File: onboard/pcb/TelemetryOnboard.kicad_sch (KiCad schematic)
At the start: 138 parts, among them J1 USB-C, J2 USB-C, J3 RFPC-SMA28-F, J4 RFPC-SMA28-F, J5 Molex_MicroFit_2pin, M1 M4 Mounting Hole, M2 M4 Mounting Hole, M3 M4 Mounting Hole, M4 M4 Mounting Hole, Q1 NPN, U1 CP2102N, U2 CP2102N, U3 RC1780HP-RC232, U4 RC1701HP-RC232, U5 AVR128DB64x-xPT, U6 W25Q80DVSSIG

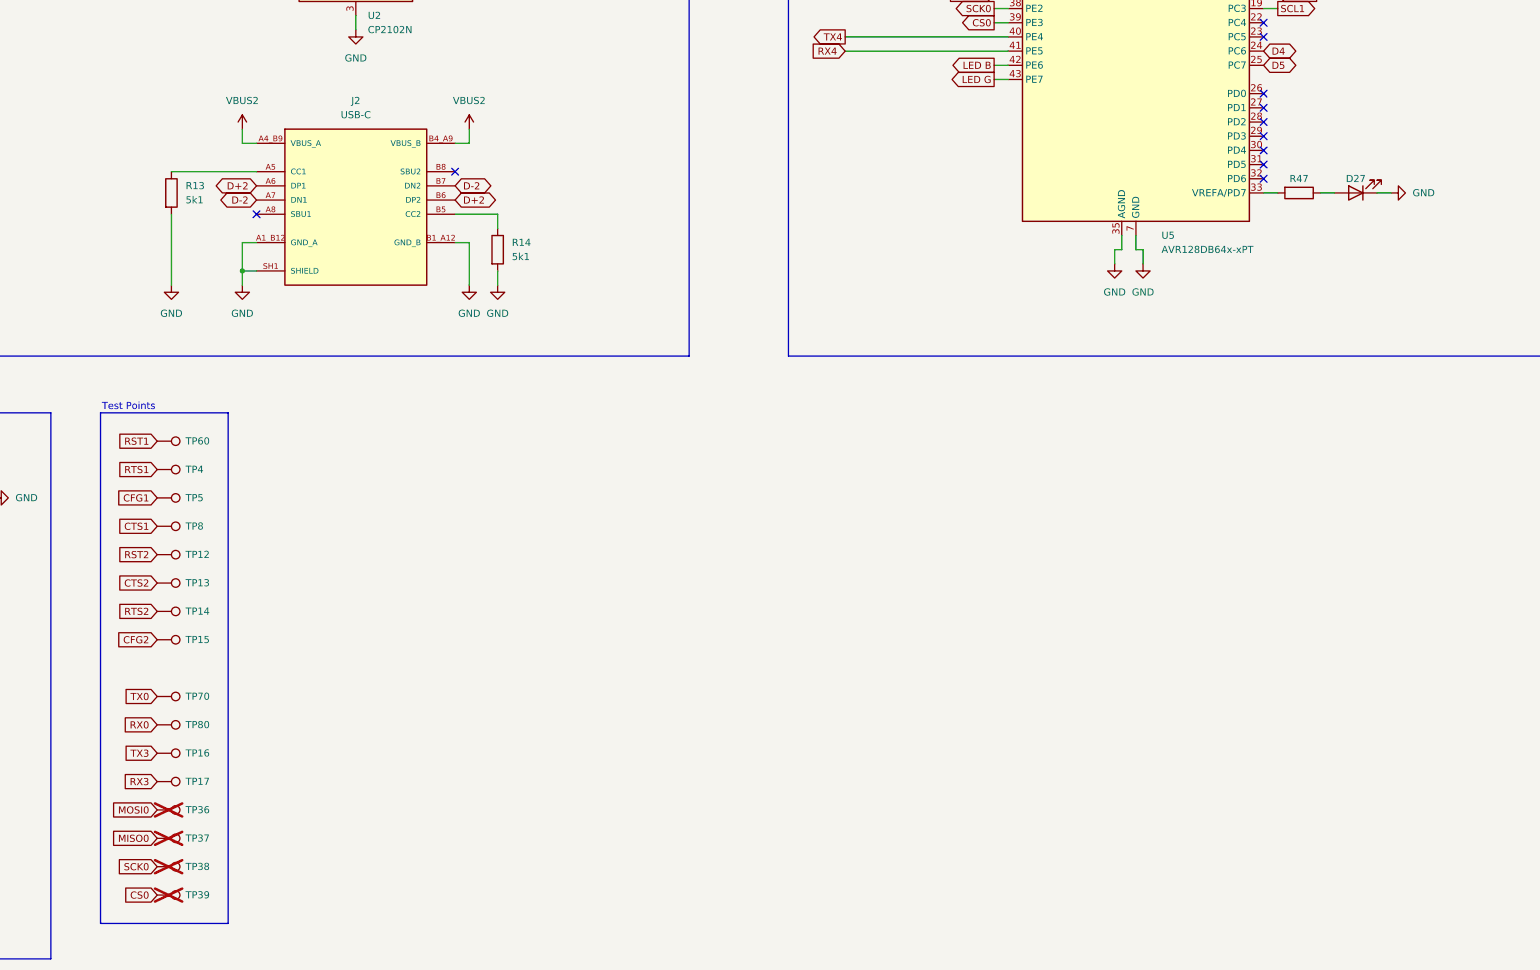
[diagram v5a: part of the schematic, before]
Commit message: improve pcb layout
include for example LEDs for three subsystems
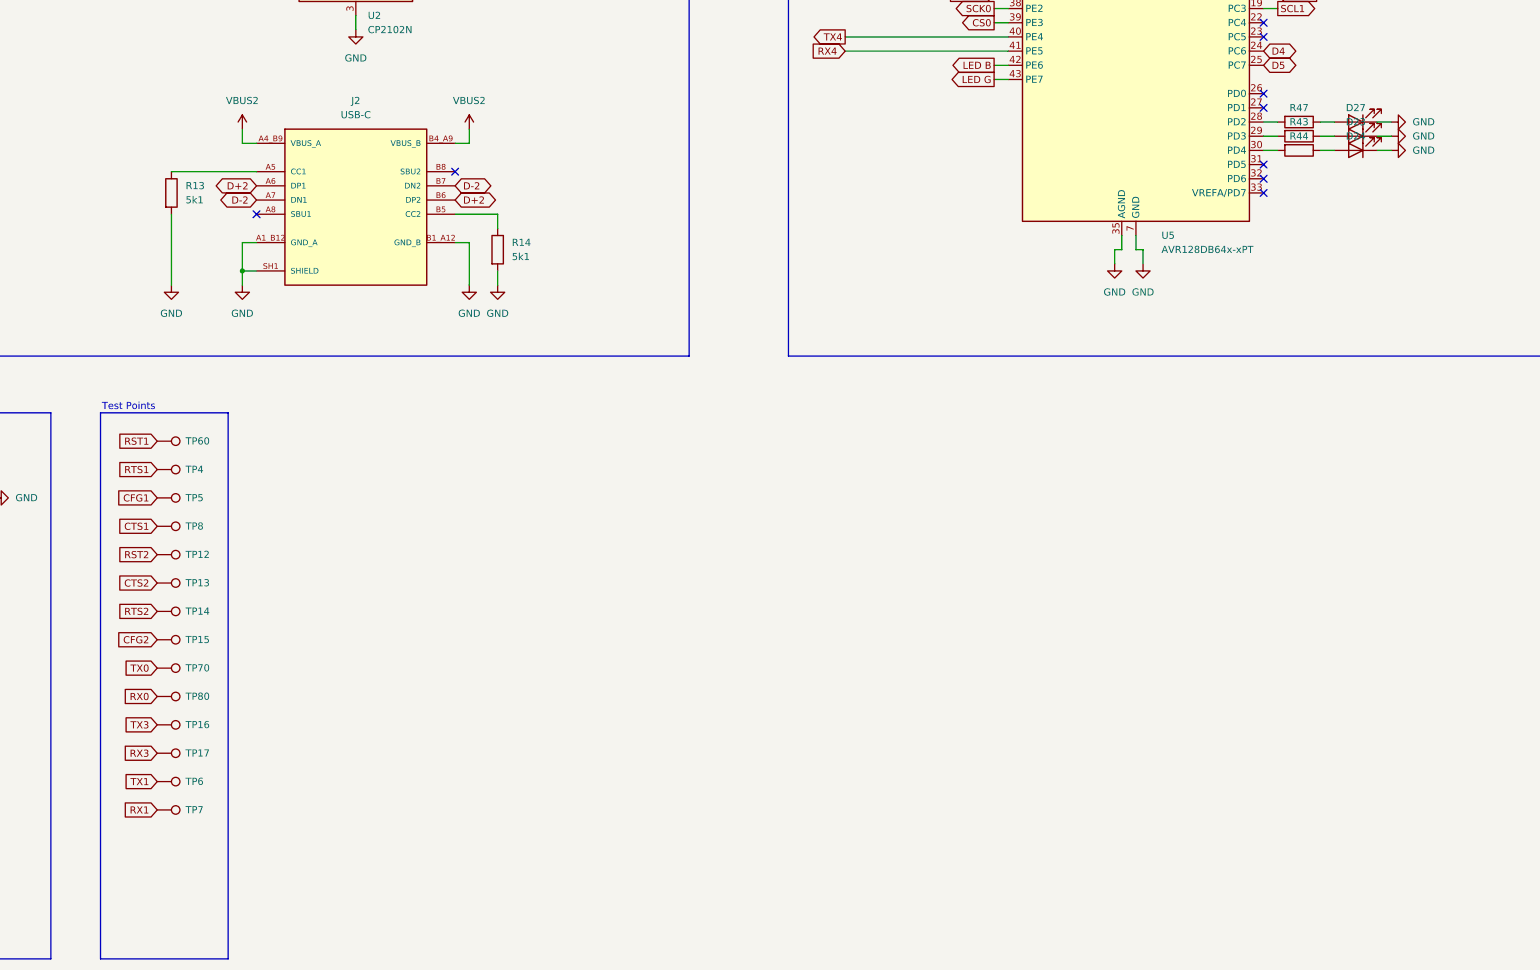
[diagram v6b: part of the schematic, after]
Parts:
- removed TP36, TP37, TP38, TP39: TestPoint, Footprints:Test Point, symbol Connector:TestPoint
- added D23, D24: orange, LED_SMD:LED_0805_2012Metric_Pad1.15x1.40mm_HandSolder, symbol Device:LED
- added R43, R44: 270R, Resistor_SMD:R_0805_2012Metric_Pad1.20x1.40mm_HandSolder, symbol Device:R
- added TP6, TP7: TestPoint, Footprints:Test Point, symbol Connector:TestPoint
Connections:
- net GND: now also D23.1 (K), D24.1 (K)
- net RX1: now also TP7.1
- net TX1: now also TP6.1
- net at U5.28 (PD2): now also R47.2
- net at U5.29 (PD3): now also R43.2
- net at U5.30 (PD4): now also R44.2
- net at U5.33 (VREFA/PD7): no longer R47.2
- new net: D24.2 (A), R44.1
- new net: D23.2 (A), R43.1
- no-connect marks 40 -> 38
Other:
- moved on the sheet: D27, R47, TP16, TP17, TP70, TP80

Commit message: smal updates and component annotation
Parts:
- removed TP4, TP5, TP60: TestPoint, Footprints:Test Point, symbol Connector:TestPoint
- added TP15, TP16, TP17: TestPoint, Footprints:Test Point, symbol Connector:TestPoint
- C10: renamed from C6; value 1 uf -> 1 uF
- C11: renamed from C7; Purchase-URL https://www.digikey.de/de/products/detail/samsung-electro-m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 -> (none)
- C12: renamed from C8; value 1 uf -> 1 uF
- C13: renamed from C15; value 1 uf -> 1 uF
- C5: renamed from C9; Purchase-URL https://www.digikey.de/de/products/detail/samsung-electro-m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 -> (none)
- C6: renamed from C10; Purchase-URL https://www.digikey.de/de/products/detail/samsung-electro-m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 -> (none)
- C7: renamed from C11; Purchase-URL https://www.digikey.de/de/products/detail/samsung-electro-m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 -> (none)
- C8: renamed from C12; Purchase-URL https://www.digikey.de/de/products/detail/samsung-electro-m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 -> (none)
- C9: renamed from C5; Purchase-URL https://www.digikey.de/de/products/detail/samsung-electro-m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 -> (none)
- D15: renamed from D23; Purchase-URL https://www.digikey.de/de/products/detail/liteon/LTST-C170K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 -> (none)
- D16: renamed from D24; Purchase-URL https://www.digikey.de/de/products/detail/liteon/LTST-C170K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 -> (none)
- D17: renamed from D27; Purchase-URL https://www.digikey.de/de/products/detail/liteon/LTST-C170K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 -> (none)
- D18: renamed from D25; Purchase-URL https://www.digikey.de/de/products/detail/liteon/LTST-C170K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 -> (none)
- D19: renamed from D26; Purchase-URL https://www.digikey.de/de/products/detail/liteon/LTST-C170K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 -> (none)
- D20, D22, D29: Purchase-URL https://www.digikey.de/de/products/detail/liteon/LTST-C171K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 -> (none)
- D21: renamed from D19; Purchase-URL https://www.digikey.de/de/products/detail/liteon/LTST-C171K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 -> (none)
- D23: renamed from D21; Purchase-URL https://www.digikey.de/de/products/detail/liteon/LTST-C171K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 -> (none)
- D24: renamed from D15; Purchase-URL https://www.digikey.de/de/products/detail/liteon/LTST-C171Y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 -> (none)
- D25: renamed from D14; Purchase-URL https://www.digikey.de/de/products/detail/liteon/LTST-C171G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 -> (none)
- D26: renamed from D17; Purchase-URL https://www.digikey.de/de/products/detail/liteon/LTST-C171Y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 -> (none)
- D27: renamed from D16; Purchase-URL https://www.digikey.de/de/products/detail/liteon/LTST-C171G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 -> (none)
- D28: renamed from D30; Purchase-URL https://www.digikey.de/de/products/detail/liteon/LTST-C171K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 -> (none)
- R1, R11, R12, R17, R2, R20, R21, R3, R4, R5, R6: value 560 Ohm -> 560R
- R18, R19: value 470 Ohm -> 470R
- R22: renamed from R29; value 180 R -> 180R
- R32: renamed from R23; Purchase-URL https://www.digikey.de/de/products/detail/yageo/RC0805JR-07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 -> (none)
- R34: renamed from R26; Purchase-URL https://www.digikey.de/de/products/detail/yageo/RC0805JR-07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 -> (none)
- R36: renamed from R43; value 270R -> 560R; Purchase-URL https://www.digikey.de/de/products/detail/yageo/RC0805JR-07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 -> (none)
- R37: renamed from R44; value 270R -> 560R; Purchase-URL https://www.digikey.de/de/products/detail/yageo/RC0805JR-07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 -> (none)
- R38: renamed from R47; value 270R -> 560R; Purchase-URL https://www.digikey.de/de/products/detail/yageo/RC0805JR-07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 -> (none)
- R39: renamed from R45; value 270R -> 560R; Purchase-URL https://www.digikey.de/de/products/detail/yageo/RC0805JR-07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 -> (none)
- R40: renamed from R46; value 270R -> 560R; Purchase-URL https://www.digikey.de/de/products/detail/yageo/RC0805JR-07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 -> (none)
- R41: renamed from R33; Purchase-URL https://www.digikey.de/de/products/detail/yageo/RC0805JR-13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 -> (none)
- R42: renamed from R32; Purchase-URL https://www.digikey.de/de/products/detail/yageo/RC0805JR-13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 -> (none)
- R43: renamed from R36; Purchase-URL https://www.digikey.de/de/products/detail/yageo/RC0805JR-13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 -> (none)
- R44: renamed from R35; Purchase-URL https://www.digikey.de/de/products/detail/yageo/RC0805JR-13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 -> (none)
- R45: renamed from R25; Purchase-URL https://www.digikey.de/de/products/detail/yageo/RC0805JR-07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 -> (none)
- R46: renamed from R24; Purchase-URL https://www.digikey.de/de/products/detail/yageo/RC0805JR-07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 -> (none)
- R47: renamed from R28; Purchase-URL https://www.digikey.de/de/products/detail/yageo/RC0805JR-07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 -> (none)
- R48: renamed from R27; Purchase-URL https://www.digikey.de/de/products/detail/yageo/RC0805JR-07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 -> (none)
- R49: renamed from R51; Purchase-URL https://www.digikey.de/de/products/detail/yageo/RC0805JR-13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 -> (none)
- R50: renamed from R22; Purchase-URL https://www.digikey.de/de/products/detail/yageo/RC0805JR-13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 -> (none)
- U5: renamed from U4; Purchase-URL https://www.digikey.de/de/products/detail/radiocrafts-as/RC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 -> (none)
- renumbered D18 to D14, R30 to R23, R31 to R24, R49 to R25, R50 to R26, R34 to R27, R41 to R28, R37 to R29, R40 to R30, R42 to R31, R38 to R33, R39 to R35, TP80 to TP10, TP6 to TP11, TP7 to TP12, TP16 to TP13, TP17 to TP14, TP8 to TP4, TP12 to TP5, TP13 to TP6, TP14 to TP7, TP15 to TP8, TP70 to TP9, U5 to U3, U3 to U4
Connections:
- net CFG1: now also TP6.1
- net CFG2: now also TP11.1; no longer TP8.1
- net CTS1: now also TP7.1; no longer TP4.1
- net CTS2: now also TP9.1; no longer TP6.1
- net RST1: now also TP4.1
- net RST2: now also TP8.1; no longer TP5.1
- net RTS1: now also TP5.1
- net RTS2: now also TP10.1; no longer TP7.1
- net RX0: now also TP13.1; no longer TP10.1
- net RX1: now also TP15.1; no longer TP12.1
- net RX3: now also TP17.1; no longer TP14.1
- net TX0: now also TP12.1; no longer TP9.1
- net TX1: now also TP14.1; no longer TP11.1
- net TX3: now also TP16.1; no longer TP13.1
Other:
- moved on the sheet: TP10, TP11, TP12, TP13, TP14, TP4, TP5, TP6, TP7, TP8, TP9

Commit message: rework schematic, add D and Q value
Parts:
- removed Q1: NPN, Package_TO_SOT_SMD:SOT-23, symbol Simulation_SPICE:NPN
- added Q1: MMBT4401-TP, Package_TO_SOT_SMD:SOT-23, symbol Symbols:MMBT4401-TP
- D14: value D -> MMSD4148T1G
- LS1: value Buzzer CMT-0525-75-SMT-TR -> CMT-0525-75-SMT-TR
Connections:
- net GND: now also Q1.2 (E)
- net LED_SENS: now reaches R37.2, U3.30 (PD4)
- net at D14.2 (A), LS1.N: now also Q1.3 (C)
- net LED_DBG1: now reaches R39.2, U3.14 (PB6)
- net LED_DBG2: now reaches R40.2, U3.15 (PB7)
- net LED_IGN: now reaches R38.2, U3.28 (PD2)
- net LED_PWR: now reaches R36.2, U3.29 (PD3)
- net at R22.1: now also Q1.1 (B)
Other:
- note added: "Debug LEDs"
- note added: "Flash Storage Chip"
- note added: "Pin Sockets / PCB Bus"
- note added: "Subsystem LEDs"
- note removed: "Flash Storage"
- note removed: "Pinheader / PCB Bus"
- note removed: "Pinheader?"
- moved on the sheet: C1, C10, C11, C12, C13, C2, C3, C4, C5, C6, C7, C8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
